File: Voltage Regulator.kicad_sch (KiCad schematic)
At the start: 4 parts, among them U4 AP2112K-3.3TRG1

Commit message: feat: Add metadata for schematic sheets
Original-author: Ishan Karmakar <ishan.karmakar24@gmail.com>
Source-commit: c82f4670f2f6b6f19a8645b0d3909227ee38d77d
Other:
- company: (none) -> Vynte
- title: (none) -> Voltage Regulator
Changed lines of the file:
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@@
 	(generator_version "10.0")
 	(paper "A5")
+	(title_block
+		(title "Voltage Regulator")
+		(date "2026-08-21")
+		(rev "${PROJECT_REV}")
+		(company "Vynte")
+	)
 	(junction
 		(at 115.57 58.42)

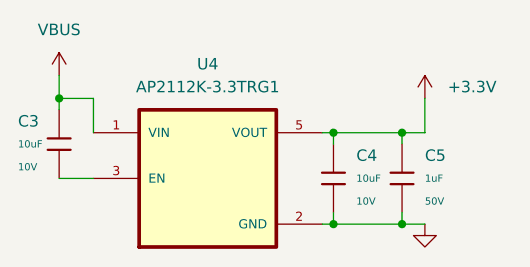
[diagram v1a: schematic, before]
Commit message: feat: Use standard KiCad capacitor symbols and footprints
Original-author: Ishan Karmakar <ishan.karmakar24@gmail.com>
Source-commit: 6d92738db7c1a3a0126f93a2d140869e5f4c1fb9
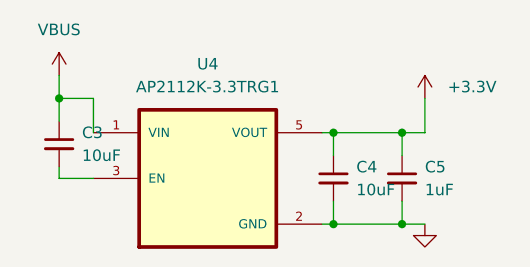
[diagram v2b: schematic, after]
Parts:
- removed C3, C4: 10uF, PCM_JLCPCB:C_0603, symbol PCM_JLCPCB-Capacitors:0603,10uF
- removed C5: 1uF, PCM_JLCPCB:C_0603, symbol PCM_JLCPCB-Capacitors:0603,1uF
- added C3, C4: 10uF, Capacitor_SMD:C_0603_1608Metric, symbol Device:C_Small
- added C5: 1uF, Capacitor_SMD:C_0603_1608Metric, symbol Device:C_Small
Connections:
- net +3.3V: now also C4.1, C5.1
- net GND: now also C4.2, C5.2
- net VBUS: now also C3.1
- net at U4.3 (EN): now also C3.2
